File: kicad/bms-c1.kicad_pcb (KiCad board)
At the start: 4 copper layers, 135 x 70 mm, 207 parts, among them J1 MicroFit 2x12, J2 B4B-PH-SM4, J3 USB_B_Micro, J4 B3B-PH-SM4, J5 B2B-PH-SM4, J6 B4B-PH-SM4, P1 CONN_01X01, P2 CONN_01X01, P3 CONN_01X01, P4 CONN_01X01, P5 CONN_01X01, Q1 DMN10H220LE, Q10 BSS84, Q11 BSS123N, Q12 ZXMP10A17GTA, Q2 IPT015N10N5, Q3 IPT015N10N5, Q4 IPT015N10N5, Q5 IPT015N10N5, Q6 IPT015N10N5, Q7 IPT015N10N5, Q8 IPT015N10N5, Q9 IPT015N10N5, U2 LMR16030, U3 SN65HVD230, U4 BQ76952, U5 ESP32-C3-MINI-1

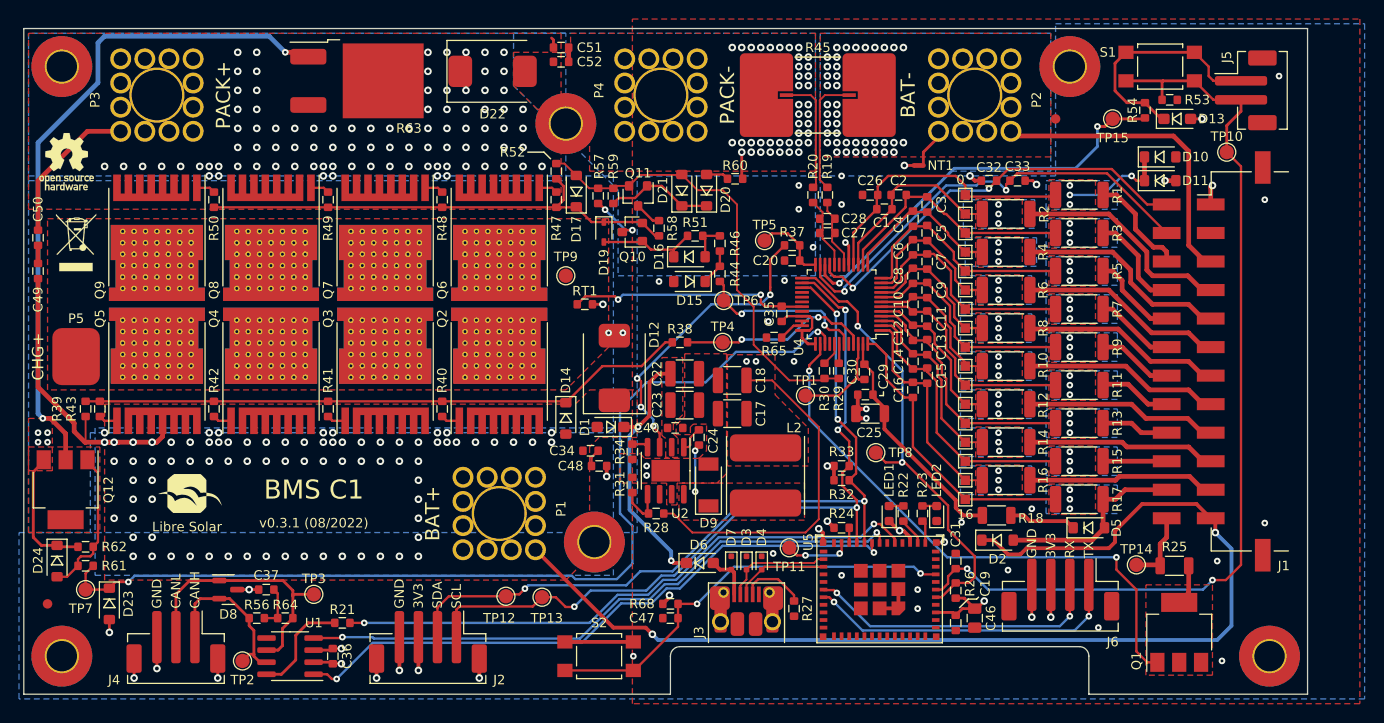
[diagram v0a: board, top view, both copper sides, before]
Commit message: Move mounting holes and improve routing
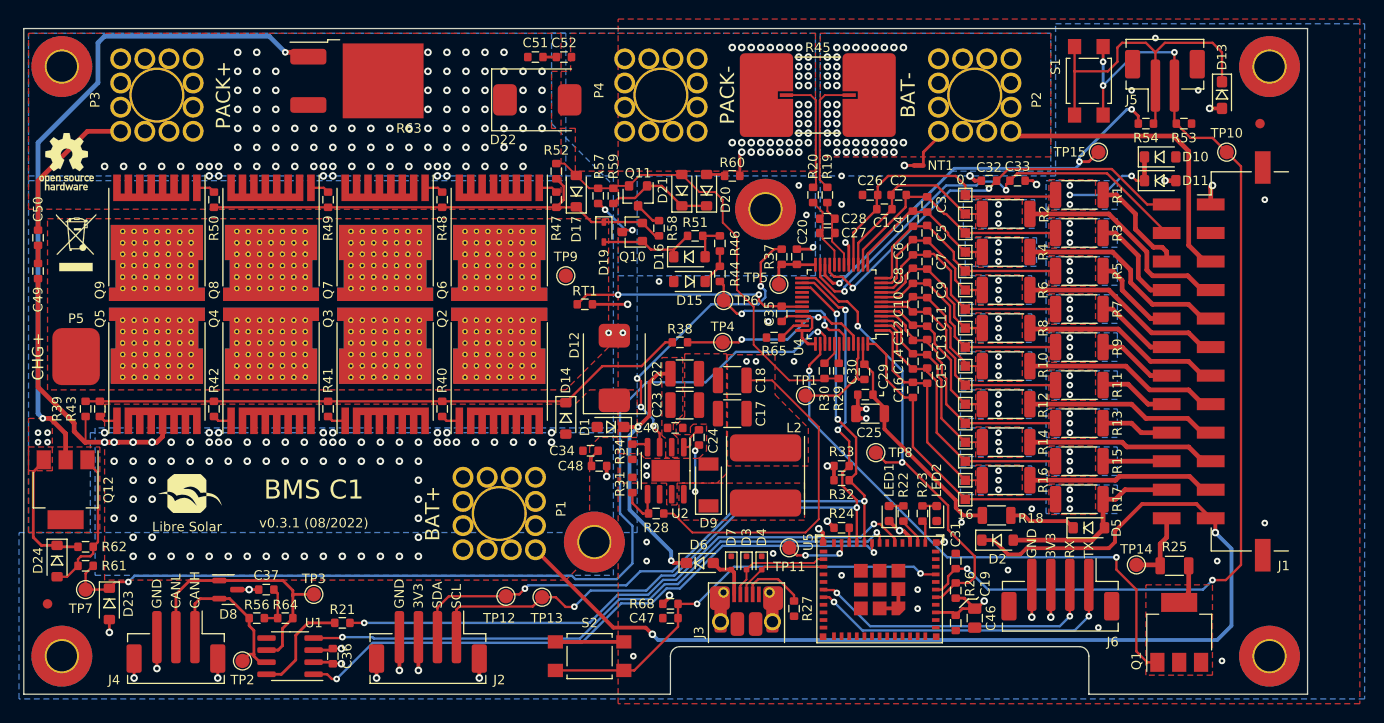
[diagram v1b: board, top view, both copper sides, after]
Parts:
- moved H2 22.8 mm to (158.0, 69.0)
- moved FID2 21.5 mm to (210.0, 60.0)
- moved H3 21.0 mm to (211.0, 54.0)
- moved J5 8.56 mm to (200.0, 55.5), turned to 0 degrees
- moved S1 7.65 mm to (192.0, 55.5), turned to -90 degrees
- moved D22 5.58 mm to (134.0, 57.5)
- moved D13 5.32 mm to (206.0, 57.0), turned to -90 degrees
- moved TP5 4.84 mm to (159.4, 76.9)
- moved TP15 3.81 mm to (193.0, 63.0)
- moved R53 2.92 mm to (202.0, 60.0)
- moved C51 2.88 mm to (133.8, 53.0)
- moved R37 1.63 mm to (159.7, 74.0), turned to -90 degrees
- moved R54 1.40 mm to (198.0, 60.0), turned to 180 degrees
- moved S2 1.00 mm to (139.5, 116.0)
- moved C20 0.64 mm to (161.3, 74.0), turned to 90 degrees
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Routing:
- net /BQ76952/BTN_HIGH: track 24.8 -> 36.7 mm
- net /BTN_LOW: track 100.6 -> 109.7 mm, vias 2 -> 5
- net GND: track 66.7 -> 71.1 mm, vias 50 -> 53
- net /BQ76952/WAKE: track 43.5 -> 46.2 mm, vias 2 -> 3
- net /REG18: track 7.96 -> 5.79 mm
- net /PACK+: track 65.2 -> 63.5 mm, vias 92 -> 100
- net /ESP32-C3 MCU/NRST: track 45.3 -> 46.3 mm

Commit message: v3.2.2: Switch to SMD terminals instead of press-fit
Rationale: These are easier to manufacture (no additional step required)
and the PCB can be mounted onto a heat sink without any milling required.
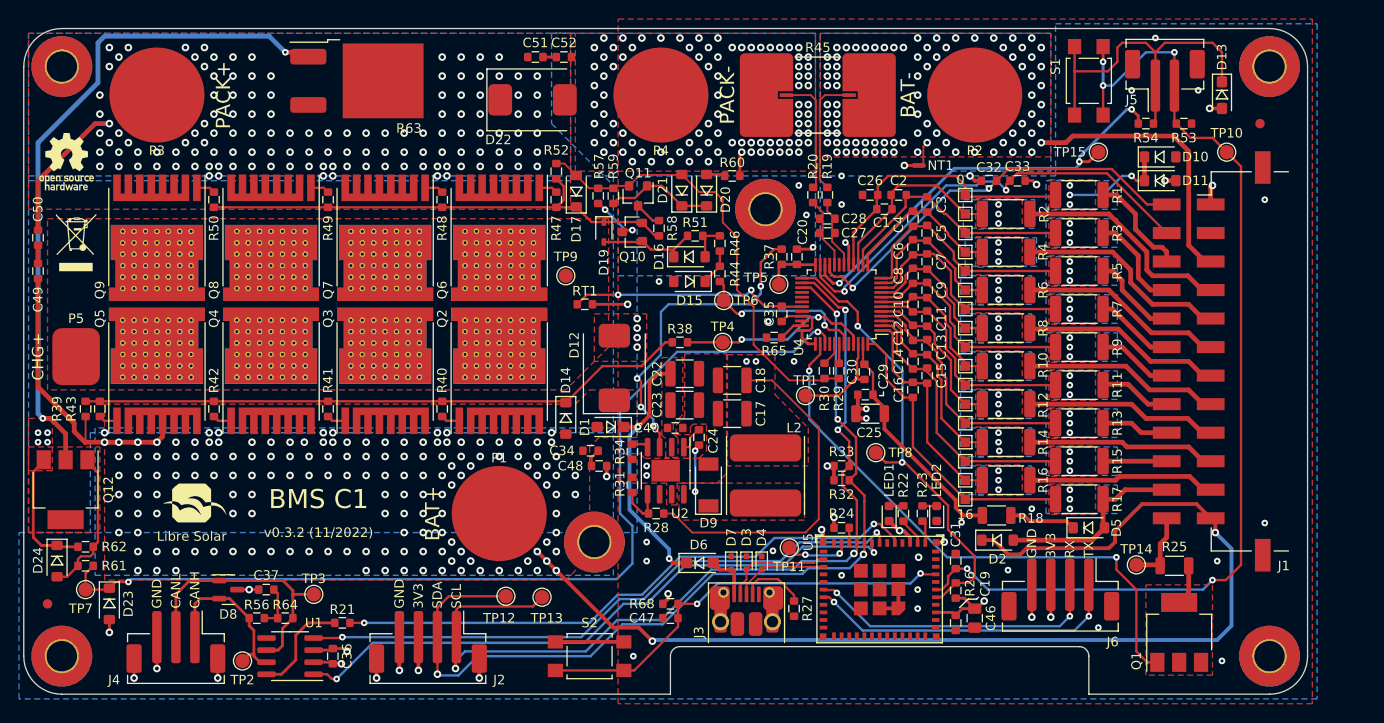
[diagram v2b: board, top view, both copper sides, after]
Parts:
- P1, P2, P3, P4: footprint LibreSolar:Wuerth_WP-BUCF_7460408_Plated -> LibreSolar:Wuerth_PowerOne_SMD_LF990005
- moved LOGO2 1.12 mm to (95.7, 101.9)
- moved D22 0.50 mm to (133.5, 57.5)
- turned P2 to 180 degrees
- turned P3 to 180 degrees
- turned P4 to 180 degrees
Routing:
- net /I2C_SCL: track 82.3 -> 96.4 mm
- net /I2C_SDA: track 83.4 -> 96.8 mm
- net /BAT-: track 36.7 -> 31.9 mm, vias 40 -> 86
- net /Power Supply/EN: track 31.9 -> 33.7 mm
- net +3V3: track 60.9 -> 61.8 mm
- net /PACK+: track 63.5 -> 62.6 mm, vias 100 -> 129
- net /ESP32-C3 MCU/NRST: track 46.3 -> 45.7 mm
- net GND: track 71.1 -> 70.9 mm, vias 53 -> 56
- net /BAT+: track 151.1 -> 151.2 mm, vias 83 -> 156
- net /PACK-: vias 40 -> 91
- added copper zone on In2.Cu, net +3V3
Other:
- outline, holes or cut-outs redrawn
- board text added: "v0.3.2 (11/2022)"
- board text removed: "v0.3.1 (08/2022)"

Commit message: v0.3.3: Final version for BMS challenge with EnAccess
Updates compared to v0.3.2:

- Optimization of some copper planes
- Net tie with thicker connection to GND
- D12 connected to Bat-

No parts were changed, the BOM is same as before.
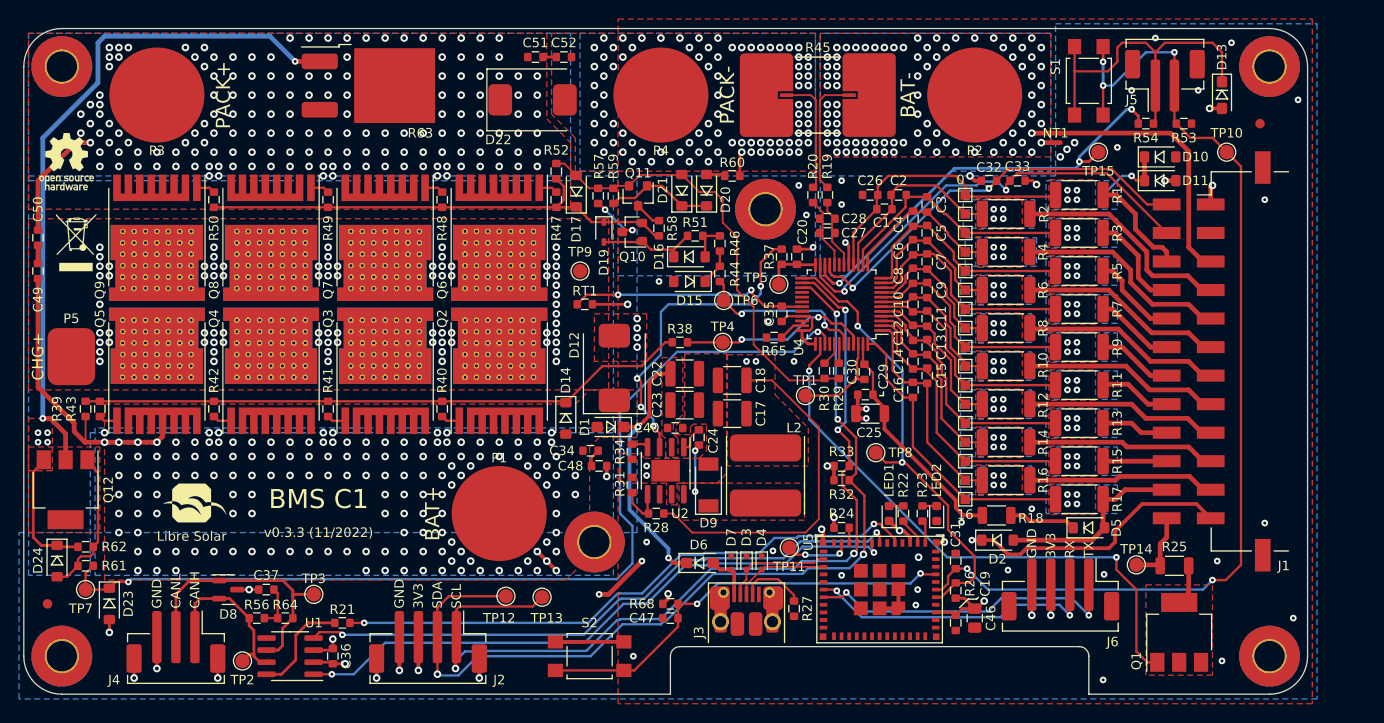
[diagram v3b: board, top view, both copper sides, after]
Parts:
- LED1: value LED -> LED red
- LED2: value LED -> LED green
- NT1: value NetTie_2 -> NetTie
- moved NT1 14.6 mm to (188.5, 62.0), turned to 0 degrees
- moved TP9 1.58 mm to (138.5, 75.5)
- moved R63 1.31 mm to (116.2, 56.0)
- moved P5 0.50 mm to (85.0, 84.5)
- renumbered H1 to H4, U3 to U1
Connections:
- C48 pad 2: GND -> /BAT-
- D12 pad 2: GND -> /BAT-
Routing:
- net +3V3: track 61.8 -> 137.7 mm, vias 10 -> 12
- net /BAT+: track 151.2 -> 119.3 mm
- net /BQ76952/VC0: track 41.4 -> 37.9 mm, vias 4 -> 5
- net /PACK+: track 62.6 -> 59.8 mm, vias 129 -> 161
- net GND: track 70.9 -> 69.1 mm, vias 56 -> 57
- net Net-(Q12-Pad2): track 71.4 -> 72.4 mm
- net /BAT-: track 31.9 -> 32.4 mm, vias 86 -> 91
- net /CHG+: vias 4 -> 82
- net /BQ76952/VC9: vias 3 -> 4
- net /BQ76952/VC8: vias 3 -> 4
- net /BQ76952/VC7: vias 3 -> 4
- net /BQ76952/VC6: vias 3 -> 4
- net /BQ76952/VC5: vias 3 -> 4
- net /BQ76952/VC4: vias 3 -> 4
- net /BQ76952/VC3: vias 3 -> 4
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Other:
- board text added: "v0.3.3 (11/2022)"
- board text removed: "v0.3.2 (11/2022)"

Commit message: v0.4.0: Multiple improvements for new board revision
- Use LMR38010 for internal power supply (max. 80V instead of 60V)
- Change USB connector from Micro-A to C and remove 5V power supply
  which was not working anyway. The board cannot be powered by USB
  only.
- Add TS2 (connected to DFETOFF) to measure shunt temperature
- Add RS-485 transceiver (sharing the connector with CAN)
- Switch I2C pins of ESP32-C3 to GPIO8/9. This allows to re-use the
  I2C pull-ups for strapping configuration and frees two pins for the
  RS-485 transceiver RE and DE pins. Also we may get rid of the I2C
  glitches during start-up.
- Use 80V instead of 100V power MOSFETs to reduce Rds(on).
- Reduce DSG gate resistor R57 to 47R to increase switch-off speed.
- Adjust some resistors to reduce number of different parts
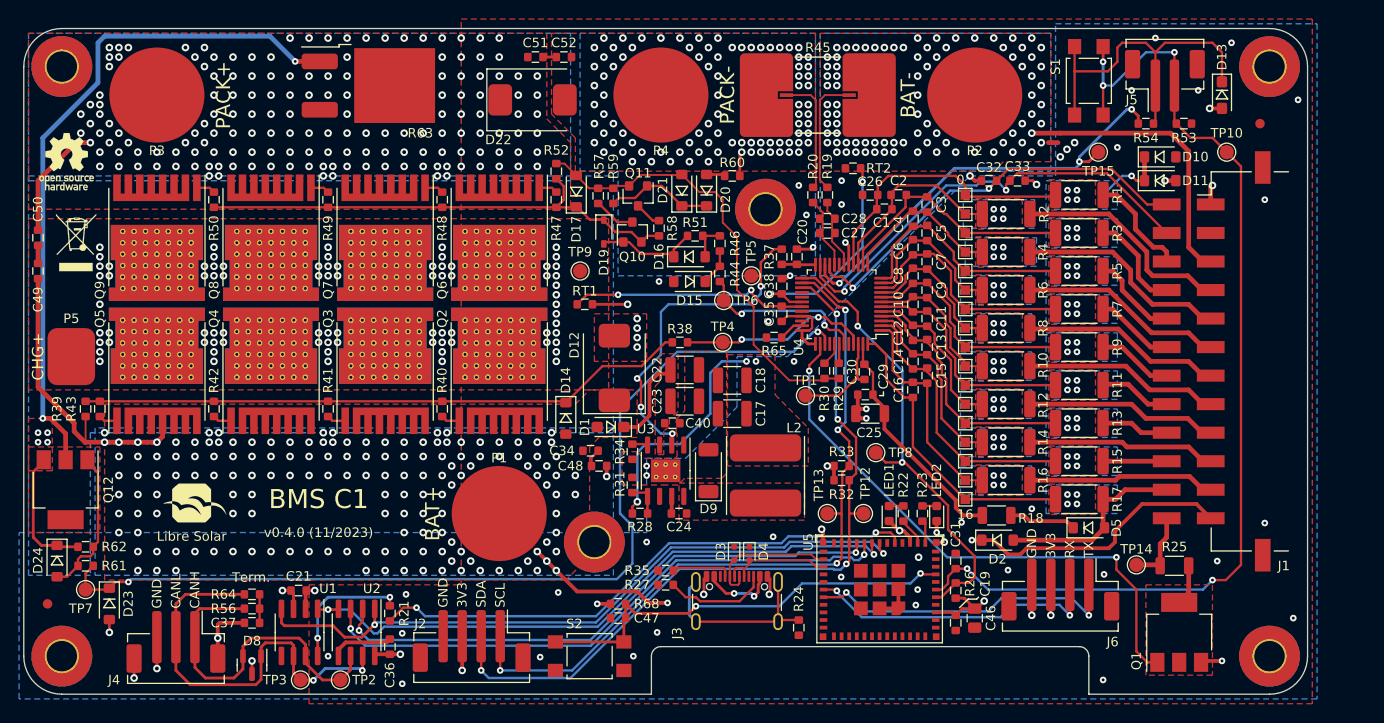
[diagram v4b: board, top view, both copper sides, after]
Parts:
- removed D6: PMEG10010ELRX, LibreSolar:D_SOD-123F
- removed D7: ESD5B5.0ST1G, LibreSolar:D_SOD-523
- removed TP11: TestPoint, TestPoint:TestPoint_Pad_D1.5mm
- added C21: 100nF, LibreSolar:C_0603_1608, F.Cu at (108.9, 109.1)
- added C38: 100pF, LibreSolar:C_0603_1608, F.Cu at (159.7, 77.1)
- added R35: 5.1k, LibreSolar:R_0603_1608, F.Cu at (147.5, 107.0)
- added RT2: 10k, LibreSolar:R_0603_1608, F.Cu at (167.2, 64.7)
- added U3: LMR38010, LibreSolar:SOIC-8-1EP_3.9x4.9mm_P1.27mm_EP2.4x3.1mm_ThermalVias, F.Cu at (147.5, 96.5)
- D12: value SMCJ60A -> SMCJ70A
- D22: value SMCJ60A -> MURS360
- J3: value USB_B_Micro -> USB_C_Receptacle_USB2.0; footprint LibreSolar:USB_Micro-B_10103594-0001LF -> Connector_USB:USB_C_Receptacle_GCT_USB4105-xx-A_16P_TopMnt_Horizontal
- L2: value 10µH -> 22µH
- Q2, Q3, Q4, Q5, Q6, Q7, Q8, Q9: value IPT015N10N5 -> IPT012N08N5
- R24: value 10k -> 1M
- R27: value 330k -> 5.1k
- R28, R65: value 100k -> 82k
- R31: value 29.4k -> 35.7k
- R34: value 49.9k -> 52.3k
- R53: value 6.8k -> 5.1k
- R54: value 4.7k -> 5.1k
- R57: value 470 -> 47
- U2: value LMR16030 -> SN65HVD75; footprint Package_SO:SOIC-8-1EP_3.9x4.9mm_P1.27mm_EP2.29x3mm -> Package_SO:SOIC-8_3.9x4.9mm_P1.27mm
- moved TP12 38.6 mm to (168.3, 101.0)
- moved U2 36.7 mm to (115.0, 113.5)
- moved TP13 31.3 mm to (164.5, 101.0)
- moved R27 13.7 mm to (147.5, 108.5), turned to 0 degrees
- moved R24 11.4 mm to (161.5, 113.0), turned to 90 degrees
- moved TP2 10.5 mm to (113.3, 118.5)
- moved TP3 9.11 mm to (109.1, 118.5)
- moved D8 8.32 mm to (104.0, 116.9), turned to -90 degrees
- moved C24 8.27 mm to (148.9, 101.0), turned to 0 degrees
- moved C36 6.08 mm to (118.5, 115.0), turned to 90 degrees
- moved C47 5.50 mm to (142.5, 112.0)
- moved R68 5.50 mm to (142.5, 110.5)
- moved R21 5.10 mm to (118.5, 111.5), turned to -90 degrees
- moved J2 4.60 mm to (127.1, 114.4)
- moved R64 4.30 mm to (104.0, 109.5), turned to 180 degrees
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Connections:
- C24 pad 1: Net-(C24-Pad1) -> Net-(U3-BOOT)
- R24 pad 1: Net-(R24-Pad1) -> GND
- R24 pad 2: +3V3 -> Net-(J3-SHIELD)
- R27 pad 1: Net-(J3-Pad4) -> GND
- R27 pad 2: GND -> Net-(J3-CC2)
- R34 pad 1: Net-(R34-Pad1) -> Net-(U3-RT/SYNC)
- TP5 pad 1: /REG18 -> /Power Supply/EN
- U2 pad 1: Net-(C24-Pad1) -> /ESP32-C3 MCU/CAN_RX
- U2 pad 2: /Power Supply/VIN -> /ESP32-C3 MCU/RS485_~{RE}
- U2 pad 3: /Power Supply/EN -> /ESP32-C3 MCU/RS485_DE
- U2 pad 4: Net-(R34-Pad1) -> /ESP32-C3 MCU/CAN_TX
- U2 pad 5: /Power Supply/FB -> GND
- U2 pad 6: unconnected-(U2-Pad6) -> /CAN_H
- U2 pad 7: GND -> /CAN_L
- U2 pad 8: /Power Supply/SW -> +3V3
- U4 pad 30: unconnected-(U4-Pad30) -> /BQ76952/TEMP_SHUNT
- U5 pad 20: /I2C_SDA -> /ESP32-C3 MCU/RS485_DE
- U5 pad 21: /I2C_SCL -> /ESP32-C3 MCU/RS485_~{RE}
- U5 pad 22: Net-(R24-Pad1) -> /I2C_SDA
- U5 pad 23: /ESP32-C3 MCU/BOOT -> /I2C_SCL
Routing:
- net /ESP32-C3 MCU/RS485_DE: track 0.00 -> 62.5 mm, vias 0 -> 2
- net /ESP32-C3 MCU/RS485_~{RE}: track 0.00 -> 60.0 mm, vias 0 -> 2
- net /BQ76952/TEMP_SHUNT: track 0.00 -> 24.0 mm, vias 0 -> 2
- net Net-(J3-SHIELD): track 0.00 -> 19.8 mm
- net /CAN_H: track 17.6 -> 35.9 mm
- net /Power Supply/VIN: track 27.2 -> 9.27 mm, vias 2 -> 0
- net /I2C_SCL: track 96.4 -> 79.1 mm
- net +3V3: track 137.7 -> 121.2 mm, vias 12 -> 11
- net /CAN_L: track 28.4 -> 44.1 mm, vias 0 -> 2
- net /I2C_SDA: track 96.8 -> 81.4 mm
- net Net-(J3-CC2): track 0.00 -> 10.9 mm
- net unconnected-(J3-VBUS-PadA4): track 0.00 -> 7.70 mm, vias 0 -> 2
- net /ESP32-C3 MCU/CAN_RX: track 65.3 -> 72.9 mm
- net Net-(J3-Pad4): track 6.93 -> 0.00 mm
- net /ESP32-C3 MCU/BOOT: track 6.90 -> 0.00 mm, vias 2 -> 0
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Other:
- outline, holes or cut-outs redrawn
- board text added: "4-layer PCB 70µm outer layers 70µm inner layers Silkscreen top only"
- board text added: "Term."
- board text added: "v0.4.0 (11/2023)"
- board text removed: "4-layer PCB 105µm outer layers 70µm inner layers Silkscreen top only"
- board text removed: "v0.3.3 (11/2022)"
